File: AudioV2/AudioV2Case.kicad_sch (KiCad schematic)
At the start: 0 parts

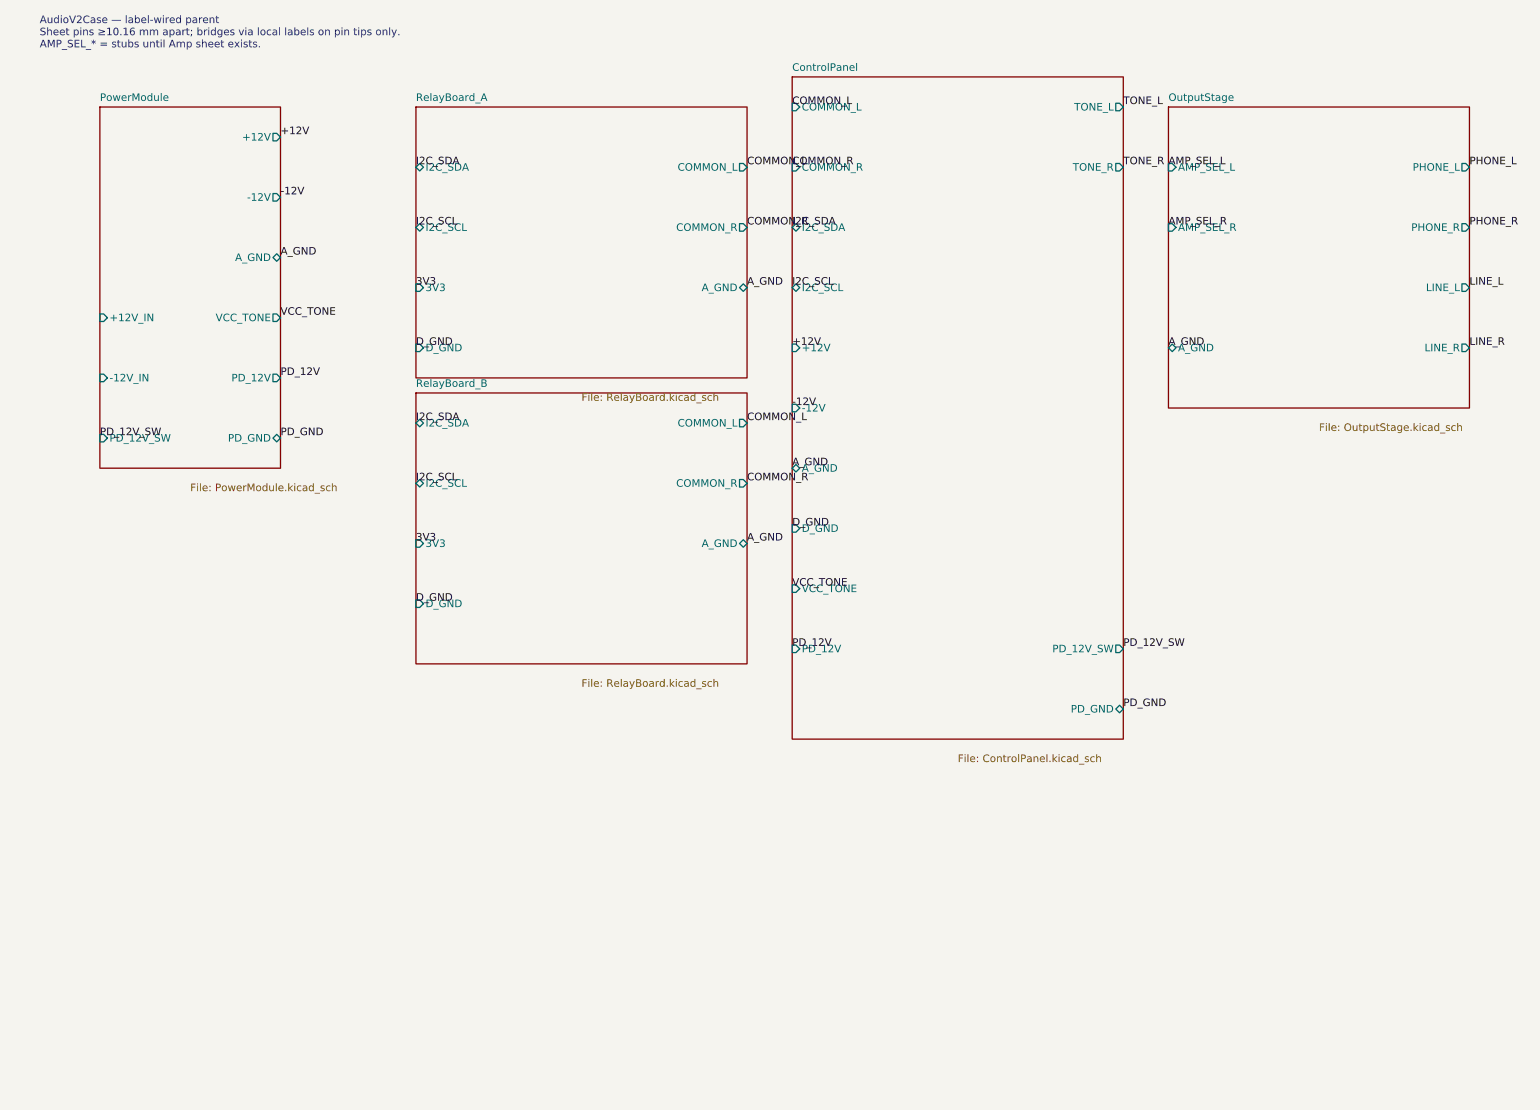
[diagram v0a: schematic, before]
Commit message: AudioV2: Power PD端子整理とエージェント引き継ぎ更新
PowerModule に J201/J202/J203 を揃え、PWR SW は ControlPanel に戻す。
AGENT_HANDOFF / WIRING に現状トポロジと PD A/B メモを残し、クラウド同期用に main へ載せる。

Co-authored-by: Cursor <cursoragent@cursor.com>
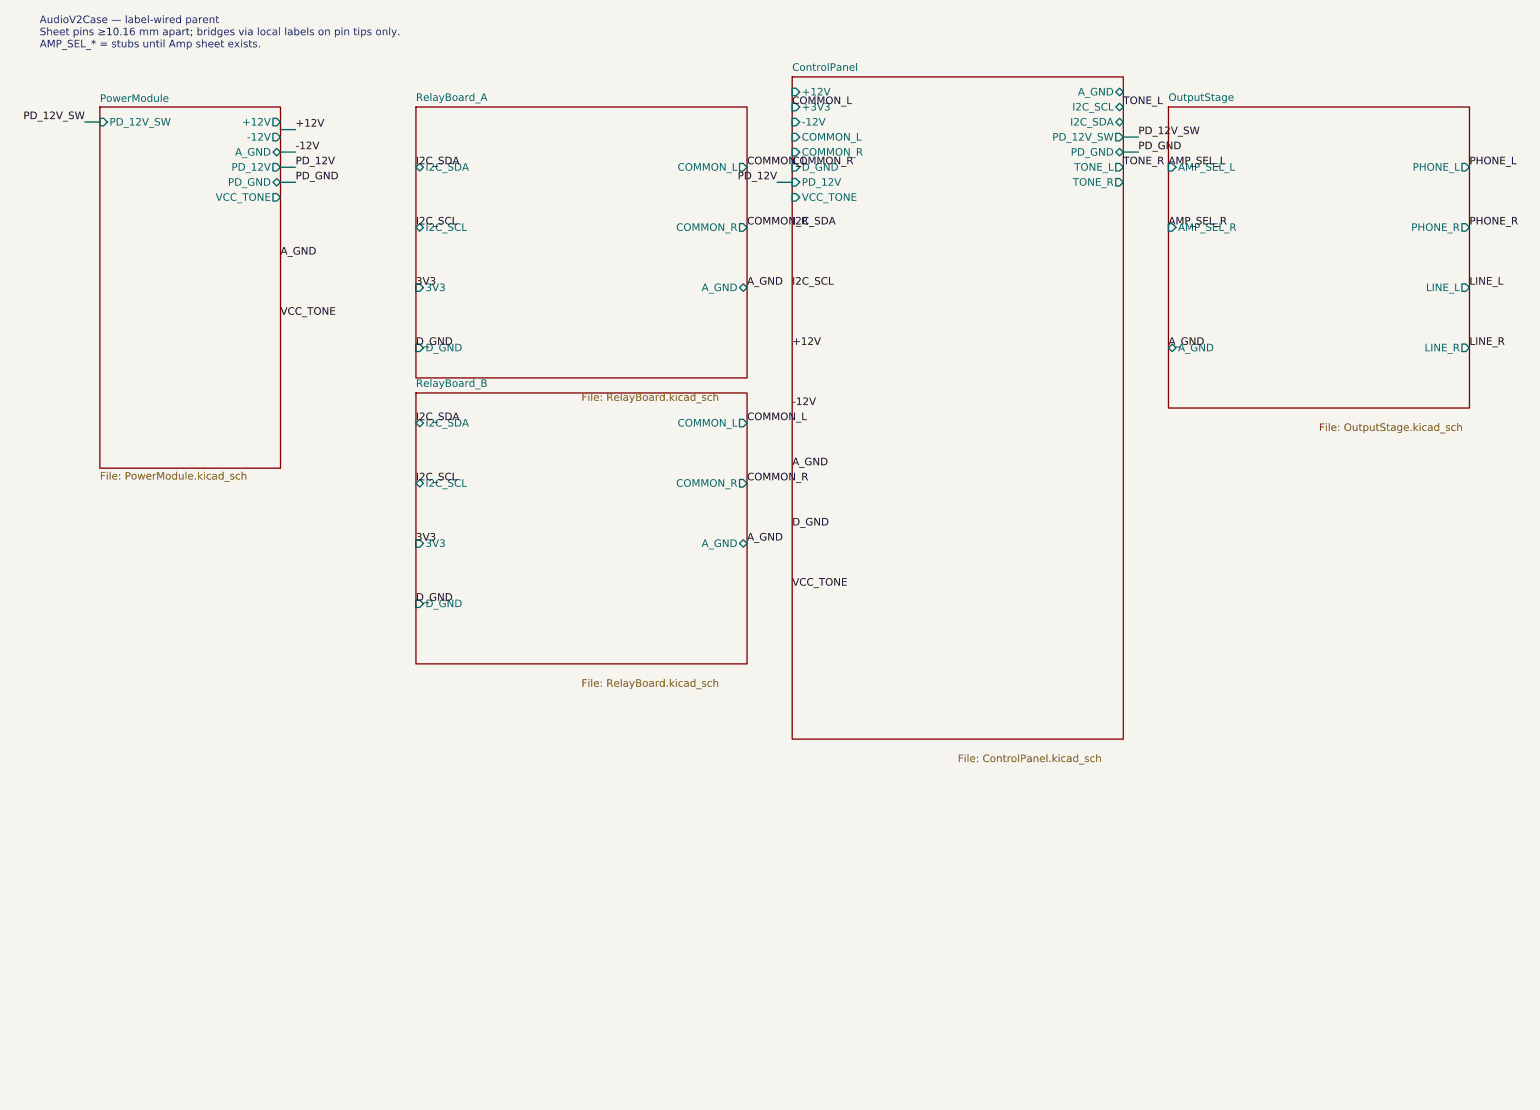
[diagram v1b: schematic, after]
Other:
- sheet ControlPanel ports: added +3V3; removed none
- sheet PowerModule ports: added none; removed +12V_IN, -12V_IN

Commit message: AudioV2: Amp再版とRelayBoard本配線、番地ストラップを0Ω化
高速オペアンプを差せるようAmpをバルク対応で再版した（ゲイン2＝20k/20k、
±12V、100µF/rail + 100nF + 1nF、DIP-8ソケット）。親には代表1シートだけ置き、
物理は同一仕様×10製造とする。PCBは既存基板の端子・4穴を維持したまま上辺を
15mm拡張してバルクを載せた。

RelayBoardは未給電Ampへ信号を印加しないよう、Amp入力と±12Vを同一の
SET/RESETで同時切替する構成で本配線した。番地はA1/A0の0Ωストラップで
0x20–0x23を選び、1枚のPCB設計を最大4枚に使い回す。SolderJumperは
FPが1.3mmピッチで0Ωチップが載らないため1206パッドに変更した。
プルダウン10kΩはジャンパ後段に置き常時実装（手前分岐だと未実装時に
A0/A1が浮く）。

ERC 207→56。Power/Output/Amp/Relay A・B は0件で、残りはControlの
未使用ピンと親の箱外ラベル。AmpのPCB DRCは電気エラー0・未配線0。

レビュー指摘（IC直近パスコン、AZ850のset voltage余裕、A0/A1ネット無名）は
未対応でAGENT_HANDOFF §2.7に記録。addr_strapのスクリプト側は現図と
非同期なので、同期までwire_circuit_design.py relayを回さない。

Co-authored-by: Cursor <cursoragent@cursor.com>
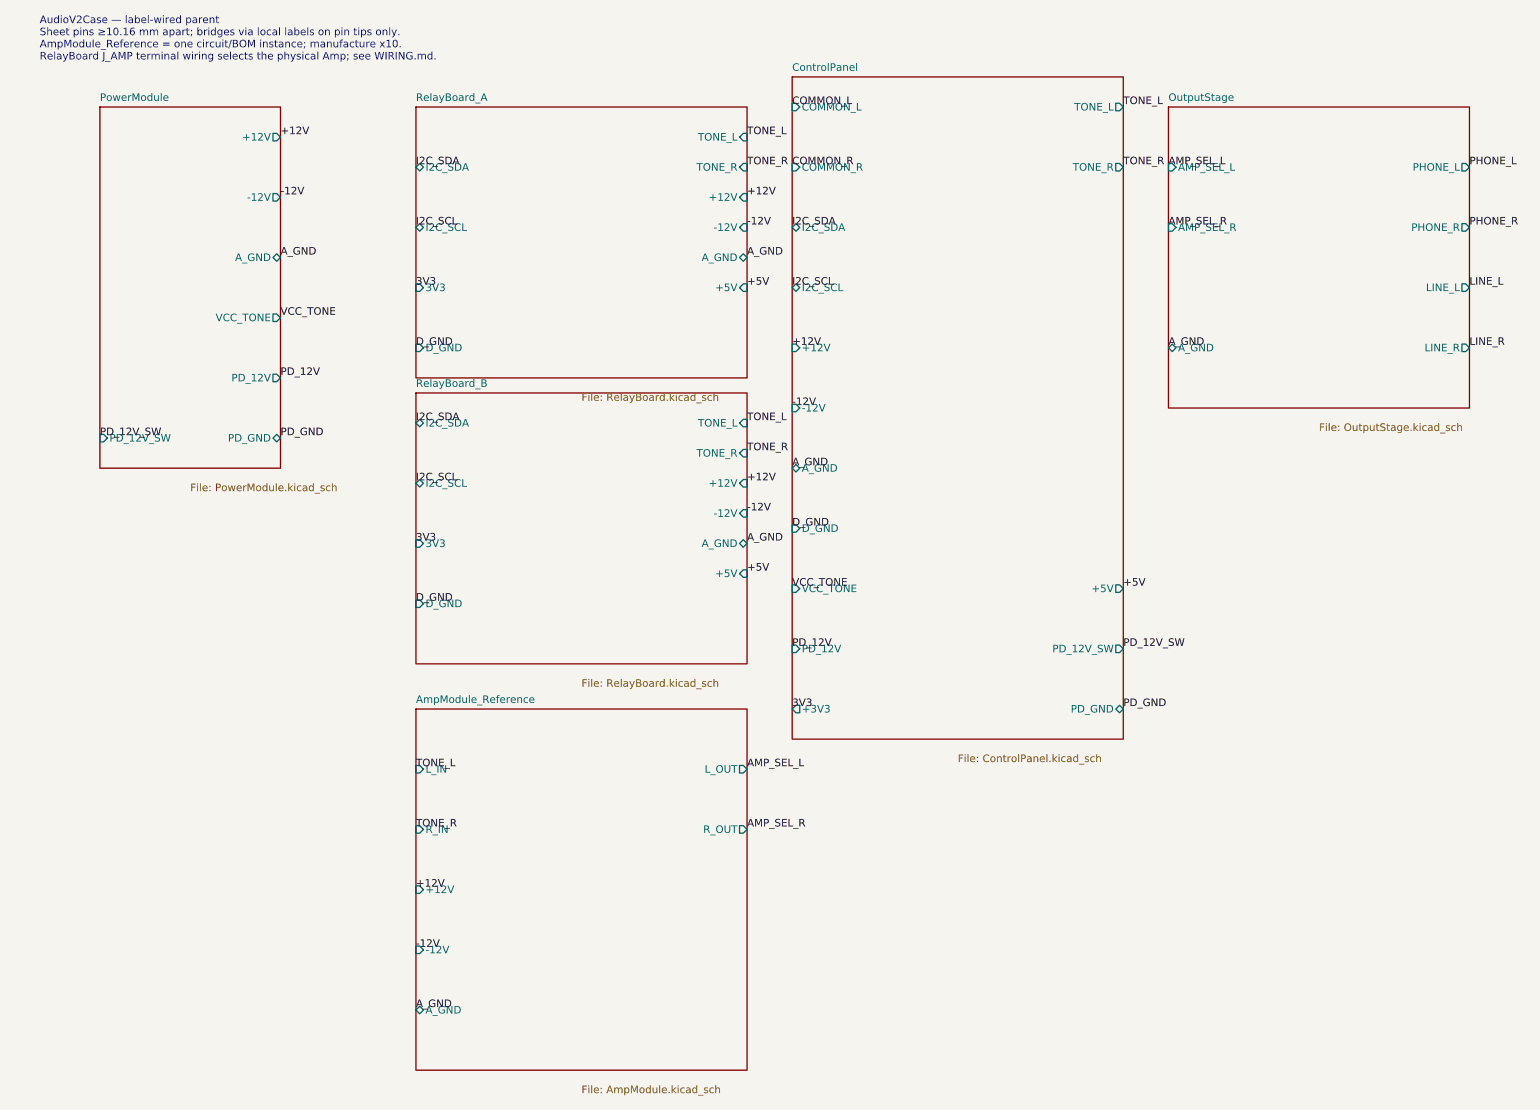
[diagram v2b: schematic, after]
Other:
- added sheet AmpModule_Reference (AmpModule.kicad_sch)
- sheet ControlPanel ports: added +5V; removed none
- sheet RelayBoard_A ports: added +12V, +5V, -12V, TONE_L, TONE_R; removed COMMON_L, COMMON_R
- sheet RelayBoard_B ports: added +12V, +5V, -12V, TONE_L, TONE_R; removed COMMON_L, COMMON_R
- note added: "AudioV2Case — label-wired parent Sheet pins ≥10.16 mm apart; bridges via local labels on pin tips only. AmpModule_Reference = one circuit/BOM instance; manufacture x10. RelayBoard J_AMP terminal wiring selects the physical Amp; see WIRING.md."
- note removed: "AudioV2Case — label-wired parent Sheet pins ≥10.16 mm apart; bridges via local labels on pin tips only. AMP_SEL_* = stubs until Amp sheet exists."
